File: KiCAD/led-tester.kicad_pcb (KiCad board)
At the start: 2 copper layers, 53.3 x 30.5 mm, 25 parts, among them IC1 ATTINY1634, P1 CONN_02X07, P2 CONN_01X02, P3 CONN_02X03, P4 CONN_01X02, SW1 SWITCH_SPDT, U1 MCP1702, U2 LM317L

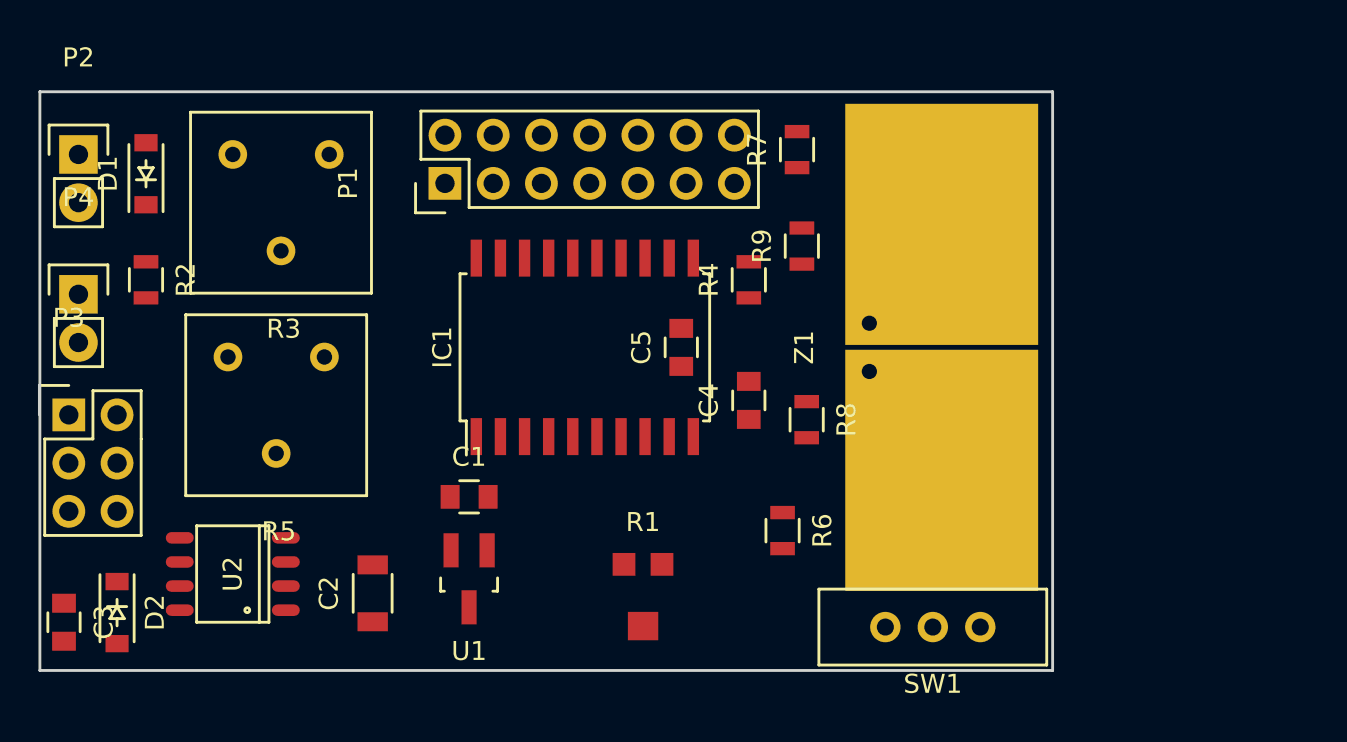
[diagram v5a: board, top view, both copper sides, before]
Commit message: updated netlist and started pcb layout
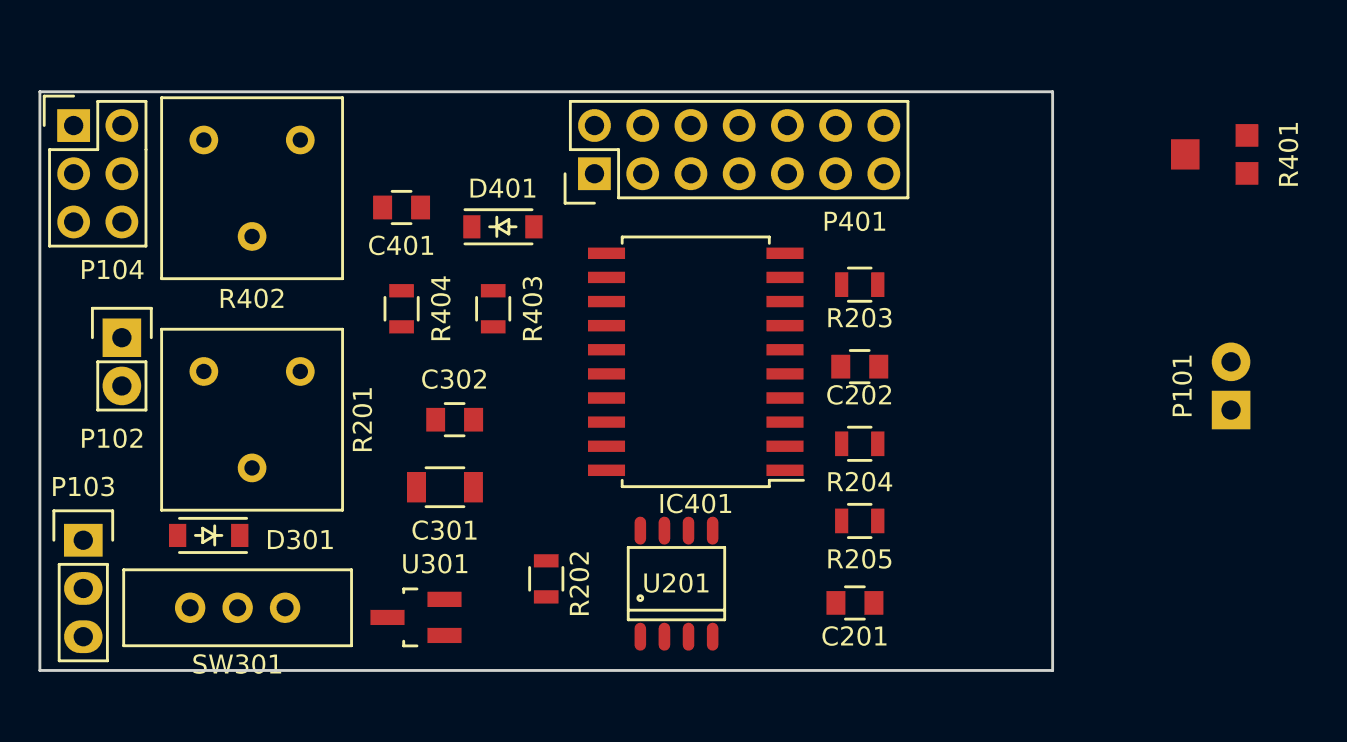
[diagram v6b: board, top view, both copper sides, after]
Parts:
- removed C1: 0.1 uF, Capacitors_SMD:C_0805
- removed C2: 2.2 uF, Capacitors_SMD:C_1206
- removed C3, C4, C5: 0.1uF, Capacitors_SMD:C_0805
- removed D1, D2: Schottky, Diodes_SMD:SOD-123
- removed IC1: ATTINY1634, led-tester:SOIC-20_7.5x12.8mm_Pitch1.27mm
- removed P1: CONN_02X07, Pin_Headers:Pin_Header_Straight_2x07
- removed P2, P4: CONN_01X02, Pin_Headers:Pin_Header_Straight_1x02
- removed P3: CONN_02X03, Pin_Headers:Pin_Header_Straight_2x03
- removed R1: 10k, led-tester:Panasonic_pot
- removed R2, R4, R8, R9: 10K, Resistors_SMD:R_0805
- removed R3: 10k, led-tester:bourns_3386_potentiometer
- removed R5: 500R, led-tester:bourns_3386_potentiometer
- removed R6, R7: 47R, Resistors_SMD:R_0805
- removed SW1: SWITCH_SPDT, led-tester:SPDT-switch
- removed U1: MCP1702, TO_SOT_Packages_SMD:SOT-23_Handsoldering
- removed U2: LM317L, Power_Integrations:SO-8
- removed Z1: testPad, led-tester:LED-LargePads
- added C201: 0.1uF, Capacitors_SMD:C_0805, F.Cu at (144.5, 77.7)
- added C202: 0.1uF, Capacitors_SMD:C_0805, F.Cu at (144.8, 65.3)
- added C301: 2.2 uF, Capacitors_SMD:C_1206, F.Cu at (122.9, 71.6)
- added C302: 0.1uF, Capacitors_SMD:C_0805, F.Cu at (123.4, 68.1)
- added C401: 0.1 uF, Capacitors_SMD:C_0805, F.Cu at (120.7, 56.9)
- added D301: Schottky, Diodes_SMD:SOD-123, F.Cu at (110.5, 74.2)
- added D401: Schottky, Diodes_SMD:SOD-123, F.Cu at (126.0, 57.9)
- added IC401: ATTINY1634, led-tester:SOIC-20_7.5x12.8mm_Pitch1.27mm, F.Cu at (136.1, 65.0)
- added P101: CONN_01X02, led-tester:LED_touch_pads, F.Cu at (164.3, 67.6)
- added P102: CONN_01X02, Pin_Headers:Pin_Header_Straight_1x02, F.Cu at (105.9, 63.8)
- added P103: CONN_01X03, Pin_Headers:Pin_Header_Straight_1x03, F.Cu at (103.9, 74.4)
- added P104: CONN_02X03, Pin_Headers:Pin_Header_Straight_2x03, F.Cu at (103.4, 52.6)
- added P401: CONN_02X07, led-tester:Pololu_diplay_2x07, F.Cu at (138.4, 53.8)
- added R201: 500R, led-tester:bourns_3386_potentiometer, F.Cu at (112.8, 68.1)
- added R202: 47R, Resistors_SMD:R_0805, F.Cu at (128.3, 76.5)
- added R203: 47R, Resistors_SMD:R_0805, F.Cu at (144.8, 61.0)
- added R204: 10K, Resistors_SMD:R_0805, F.Cu at (144.8, 69.3)
- added R205: 10K, Resistors_SMD:R_0805, F.Cu at (144.8, 73.4)
- added R401: 10k, led-tester:Panasonic_pot, F.Cu at (163.6, 54.1)
- added R402: 10k, led-tester:bourns_3386_potentiometer, F.Cu at (112.8, 55.9)
- added R403: 10K, Resistors_SMD:R_0805, F.Cu at (125.5, 62.2)
- added R404: 10K, Resistors_SMD:R_0805, F.Cu at (120.7, 62.2)
- added SW301: SWITCH_SPDT, led-tester:SPDT-switch, F.Cu at (112.0, 78.0)
- added U201: LM317L, Power_Integrations:SO-8, F.Cu at (135.1, 76.7)
- added U301: MCP1702, TO_SOT_Packages_SMD:SOT-23_Handsoldering, F.Cu at (121.4, 78.5)

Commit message: updated files
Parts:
- moved C201 14.0 mm to (145.0, 63.8)
- moved C202 8.13 mm to (145.0, 73.4)
- moved R204 7.62 mm to (145.0, 77.0)
- moved R205 5.85 mm to (145.0, 67.6)
- moved D301 4.83 mm to (115.3, 74.4)
- moved P102 3.39 mm to (105.2, 67.1), turned to 180 degrees
- turned R203 to 180 degrees
- turned SW301 to 180 degrees
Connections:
- C201 pad 2: Net-(C201-Pad2) -> GND
- C202 pad 2: Net-(C201-Pad2) -> GND
- R203 pad 2: Net-(C201-Pad2) -> GND
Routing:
- net +5V: track 0.00 -> 70.6 mm
- net /current_sensor/LED+: track 0.00 -> 64.9 mm
- net /current_sensor/LED-: track 0.00 -> 37.2 mm
- net Net-(D301-Pad2): track 0.00 -> 32.9 mm
- net +9V: track 0.00 -> 15.0 mm
- net /power/Battery+: track 0.00 -> 15.0 mm
- net /Digital Display/LEDhigh: track 0.00 -> 12.9 mm

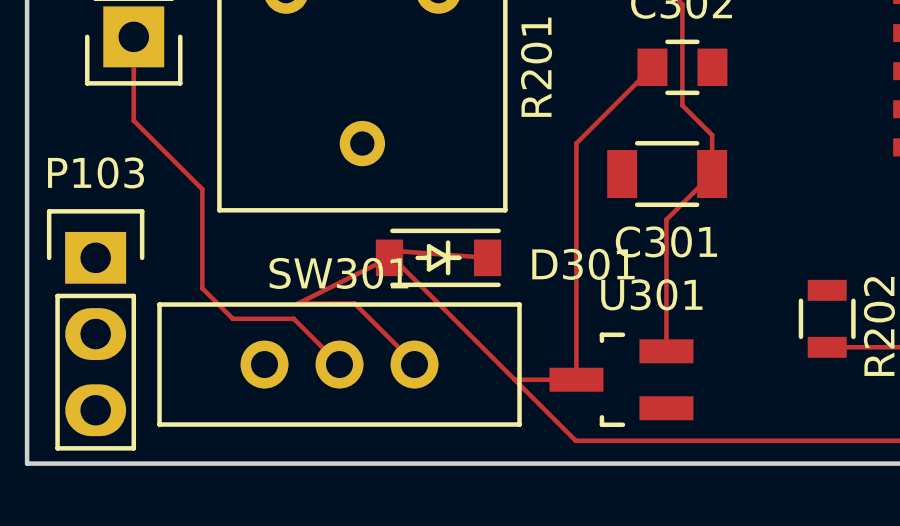
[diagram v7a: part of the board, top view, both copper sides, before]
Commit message: tried to fix the GND "not driven" messages.  Only moderately successful.
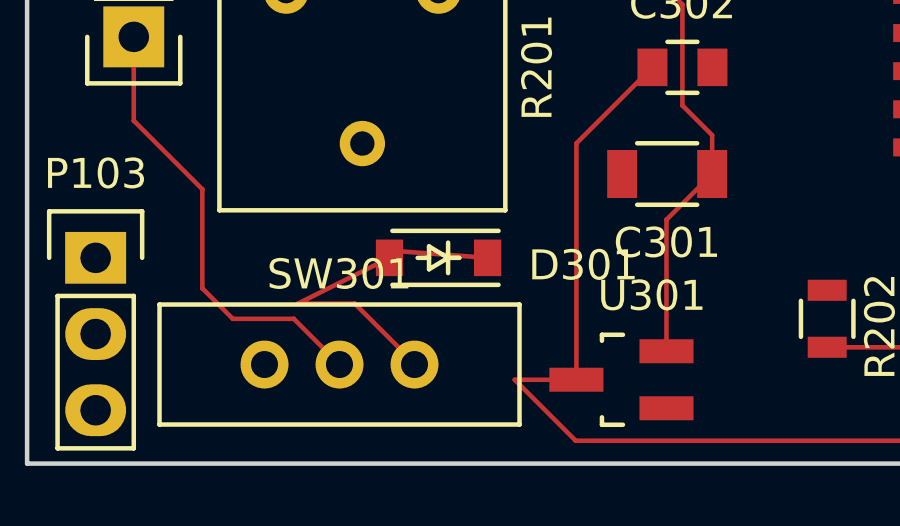
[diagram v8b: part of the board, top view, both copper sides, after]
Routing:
- net Net-(D301-Pad2): track 32.9 -> 11.6 mm
- net +9V: track 15.0 -> 30.1 mm
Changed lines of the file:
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@@
   (general
     (links 57)
-    (no_connects 37)
+    (no_connects 36)
     (area 101.524999 50.724999 155.015001 81.355001)
     (thickness 1.6)
     (drawings 4)
-    (tracks 67)
+    (tracks 66)
     (zones 0)
     (modules 25)
@@
   (segment (start 132.207 80.518) (end 133.223 79.502) (width 0.1524) (layer F.Cu) (net 3))
   (segment (start 117.856 78.486) (end 119.91086 78.486) (width 0.1524) (layer F.Cu) (net 3))
-  (segment (start 146.034 63.754) (end 146.034 63.77) (width 0.1524) (layer F.Cu) (net 4) (status C00000))
-  (segment (start 146.034 63.77) (end 144.145 65.659) (width 0.1524) (layer F.Cu) (net 4) (status 400000))
-  (segment (start 144.145 65.659) (end 140.844 65.659) (width 0.1524) (layer F.Cu) (net 4) (status 800000))
+  (segment (start 117.856 78.486) (end 119.888 80.518) (width 0.1524) (layer F.Cu) (net 3))
+  (segment (start 119.888 80.518) (end 132.207 80.518) (width 0.1524) (layer F.Cu) (net 3))
+  (segment (start 146.034 63.754) (end 146.034 63.77) (width 0.1524) (layer F.Cu) (net 4))
+  (segment (start 146.034 63.77) (end 144.145 65.659) (width 0.1524) (layer F.Cu) (net 4))
+  (segment (start 144.145 65.659) (end 140.844 65.659) (width 0.1524) (layer F.Cu) (net 4))
   (segment (start 150.368 63.5) (end 150.368 63.754) (width 0.1524) (layer F.Cu) (net 4))
   (segment (start 147.828 60.96) (end 150.368 63.5) (width 0.1524) (layer F.Cu) (net 4))
-  (segment (start 145.73 60.96) (end 147.828 60.96) (width 0.1524) (layer F.Cu) (net 4) (status 400000))
+  (segment (start 145.73 60.96) (end 147.828 60.96) (width 0.1524) (layer F.Cu) (net 4))
   (segment (start 150.368 63.754) (end 150.622 63.754) (width 0.1524) (layer F.Cu) (net 4))
-  (segment (start 145.984 67.564) (end 145.984 67.376) (width 0.1524) (layer F.Cu) (net 4) (status C00000))
-  (segment (start 145.984 67.376) (end 149.352 64.008) (width 0.1524) (layer F.Cu) (net 4) (status 400000))
+  (segment (start 145.984 67.564) (end 145.984 67.376) (width 0.1524) (layer F.Cu) (net 4))
+  (segment (start 145.984 67.376) (end 149.352 64.008) (width 0.1524) (layer F.Cu) (net 4))
   (segment (start 149.352 64.008) (end 149.352 63.754) (width 0.1524) (layer F.Cu) (net 4))
-  (segment (start 146.034 63.754) (end 149.352 63.754) (width 0.1524) (layer F.Cu) (net 4) (status 400000))
+  (segment (start 146.034 63.754) (end 149.352 63.754) (width 0.1524) (layer F.Cu) (net 4))
   (segment (start 149.352 63.754) (end 150.622 63.754) (width 0.1524) (layer F.Cu) (net 4))
   (segment (start 150.622 63.754) (end 163.068 63.754) (width 0.1524) (layer F.Cu) (net 4))
-  (segment (start 163.068 63.754) (end 164.338 65.024) (width 0.1524) (layer F.Cu) (net 4) (status 800000))
+  (segment (start 163.068 63.754) (end 164.338 65.024) (width 0.1524) (layer F.Cu) (net 4))
   (segment (start 145.73 60.96) (end 145.542 60.96) (width 0.1524) (layer F.Cu) (net 4))
   (segment (start 163.576 65.024) (end 164.338 65.024) (width 0.1524) (layer F.Cu) (net 4))
-  (segment (start 144.034 73.406) (end 144.034 67.614) (width 0.1524) (layer F.Cu) (net 5) (status C00000))
-  (segment (start 144.034 67.614) (end 144.084 67.564) (width 0.1524) (layer F.Cu) (net 5) (status C00000))
-  (segment (start 144.084 67.564) (end 143.256 67.564) (width 0.1524) (layer F.Cu) (net 5) (status 400000))
-  (segment (start 142.621 66.929) (end 140.844 66.929) (width 0.1524) (layer F.Cu) (net 5) (status 800000))
+  (segment (start 144.034 73.406) (end 144.034 67.614) (width 0.1524) (layer F.Cu) (net 5))
+  (segment (start 144.034 67.614) (end 144.084 67.564) (width 0.1524) (layer F.Cu) (net 5))
+  (segment (start 144.084 67.564) (end 143.256 67.564) (width 0.1524) (layer F.Cu) (net 5))
+  (segment (start 142.621 66.929) (end 140.844 66.929) (width 0.1524) (layer F.Cu) (net 5))
   (segment (start 143.256 67.564) (end 142.621 66.929) (width 0.1524) (layer F.Cu) (net 5))
-  (segment (start 144.084 76.962) (end 144.084 73.456) (width 0.1524) (layer F.Cu) (net 5) (status C00000))
-  (segment (start 144.084 73.456) (end 144.034 73.406) (width 0.1524) (layer F.Cu) (net 5) (status C00000))
-  (segment (start 117.856 78.486) (end 119.888 80.518) (width 0.1524) (layer F.Cu) (net 6))
-  (segment (start 119.888 80.518) (end 132.207 80.518) (width 0.1524) (layer F.Cu) (net 6))
+  (segment (start 144.084 76.962) (end 144.084 73.456) (width 0.1524) (layer F.Cu) (net 5))
+  (segment (start 144.084 73.456) (end 144.034 73.406) (width 0.1524) (layer F.Cu) (net 5))
   (segment (start 116.951 74.422) (end 113.538 74.168) (width 0.1524) (layer F.Cu) (net 6) (status 10))
-  (segment (start 113.538 74.168) (end 117.856 78.486) (width 0.1524) (layer F.Cu) (net 6))
   (segment (start 114.514 77.978) (end 114.514 77.938) (width 0.1524) (layer F.Cu) (net 6))
   (segment (start 114.514 77.938) (end 112.522 75.946) (width 0.1524) (layer F.Cu) (net 6))
   (segment (start 112.522 75.946) (end 110.633 75.946) (width 0.1524) (layer F.Cu) (net 6))
   (segment (start 110.633 75.946) (end 113.681 74.422) (width 0.1524) (layer F.Cu) (net 6) (status 20))
-  (segment (start 145.984 76.962) (end 154.94 76.962) (width 0.1524) (layer F.Cu) (net 24) (status 400000))
-  (segment (start 154.94 76.962) (end 164.338 67.564) (width 0.1524) (layer F.Cu) (net 24) (status 800000))
+  (segment (start 145.984 76.962) (end 154.94 76.962) (width 0.1524) (layer F.Cu) (net 24))
+  (segment (start 154.94 76.962) (end 164.338 67.564) (width 0.1524) (layer F.Cu) (net 24))
   (segment (start 145.73 77.52) (end 145.526 77.724) (width 0.1524) (layer F.Cu) (net 24))
   (segment (start 137.033 79.502) (end 137.033 78.613) (width 0.1524) (layer F.Cu) (net 24))
